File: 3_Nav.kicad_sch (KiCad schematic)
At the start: 37 parts, among them J401 Screw_Terminal_01x04, SW401 SW_Push, SW402 SW_Push, U401 LPS22HH, U402 MS5607, U403 STM32F412RGTx, U404 ICM-42688-P, U405 LSM6DSO32TR, Y401 YXC YSX321SL, Y402 Seiko SC-32S

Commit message: Add files via upload
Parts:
- U404: symbol ICM-42688-P:ICM-42688-P -> Polaris_symbols:ICM-42688-P
- U405: symbol LSM6DSO32TR:LSM6DSO32TR -> Polaris_symbols:LSM6DSO32TR
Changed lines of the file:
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@@
 	)
 	(symbol
-		(lib_id "LSM6DSO32TR:LSM6DSO32TR")
+		(lib_id "Polaris_symbols:LSM6DSO32TR")
 		(at 233.68 138.43 0)
 		(unit 1)
@@
 	)
 	(symbol
-		(lib_id "ICM-42688-P:ICM-42688-P")
+		(lib_id "Polaris_symbols:ICM-42688-P")
 		(at 226.06 81.28 0)
 		(unit 1)

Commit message: Added symbols and footprints Changed schematic to use footprints and symbols from added symbols and footprints
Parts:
- R407, R408: footprint (none) -> Resistor_SMD:R_0603_1608Metric
- SW401, SW402: footprint (none) -> Button_Switch_THT:SW_PUSH_6mm
- U401: footprint LPS22HHTR:HLGA-10L_2X2X0P73_STM -> Polaris:LPS22HH
- U404: footprint ICM42688-P:PQFN50P300X250X97-14N -> Polaris:ICM-42688-P
- U405: footprint LSM6DSO32TR:LSM6DSO32TR -> Polaris:LSM6DSO32TR

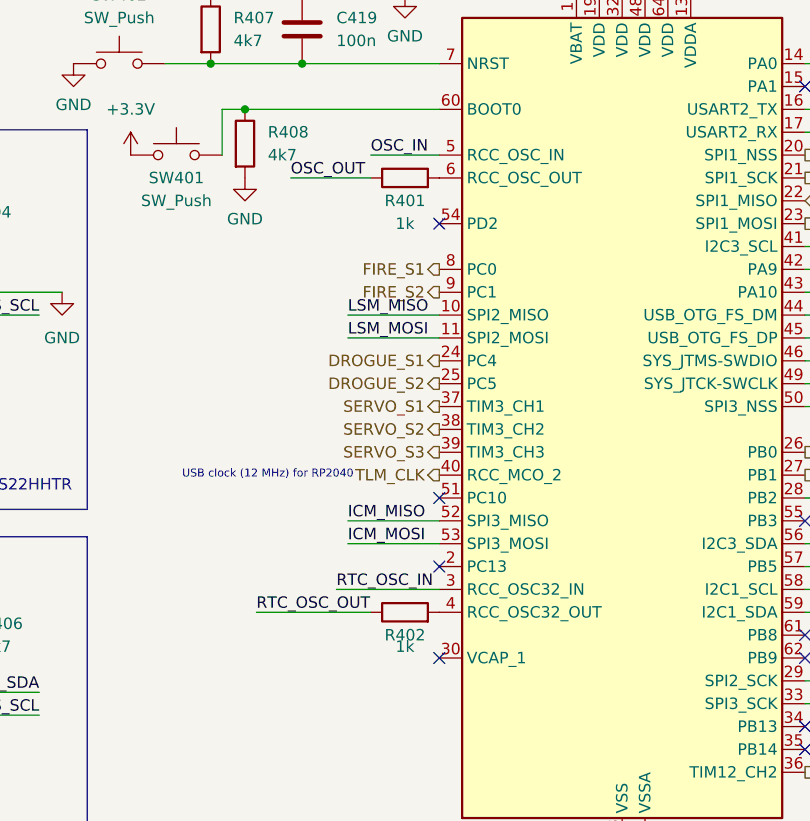
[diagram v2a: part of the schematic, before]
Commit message: Changed oscillator series resistors to DNP
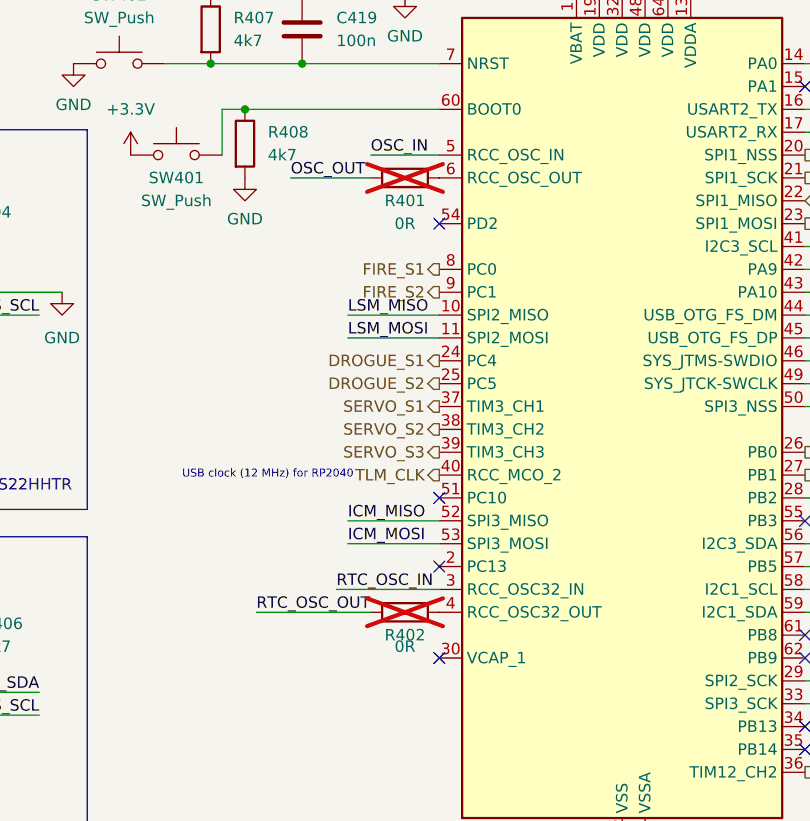
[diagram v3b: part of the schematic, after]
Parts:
- R401, R402: value 1k -> 0R; now not fitted
- Y401: footprint (none) -> Crystal:Crystal_SMD_3225-4Pin_3.2x2.5mm
- Y402: footprint (none) -> Crystal:Crystal_SMD_3215-2Pin_3.2x1.5mm
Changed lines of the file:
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@@
 			)
 		)
-		(property "Footprint" ""
+		(property "Footprint" "Crystal:Crystal_SMD_3225-4Pin_3.2x2.5mm"
 			(at 41.91 175.26 0)
 			(hide yes)
@@
 		(on_board yes)
 		(in_pos_files yes)
-		(dnp no)
+		(dnp yes)
 		(property "Reference" "R402"
 			(at 113.03 135.89 90)
@@
 			)
 		)
-		(property "Value" "1k"
+		(property "Value" "0R"
 			(at 113.03 137.16 90)
 			(show_name no)
@@
 		(on_board yes)
 		(in_pos_files yes)
-		(dnp no)
+		(dnp yes)
 		(property "Reference" "R401"
 			(at 113.03 87.63 90)
@@
 			)
 		)
-		(property "Value" "1k"
+		(property "Value" "0R"
 			(at 113.03 90.17 90)
 			(show_name no)
@@
 			)
 		)
-		(property "Footprint" ""
+		(property "Footprint" "Crystal:Crystal_SMD_3215-2Pin_3.2x1.5mm"
 			(at 90.17 175.26 0)
 			(hide yes)

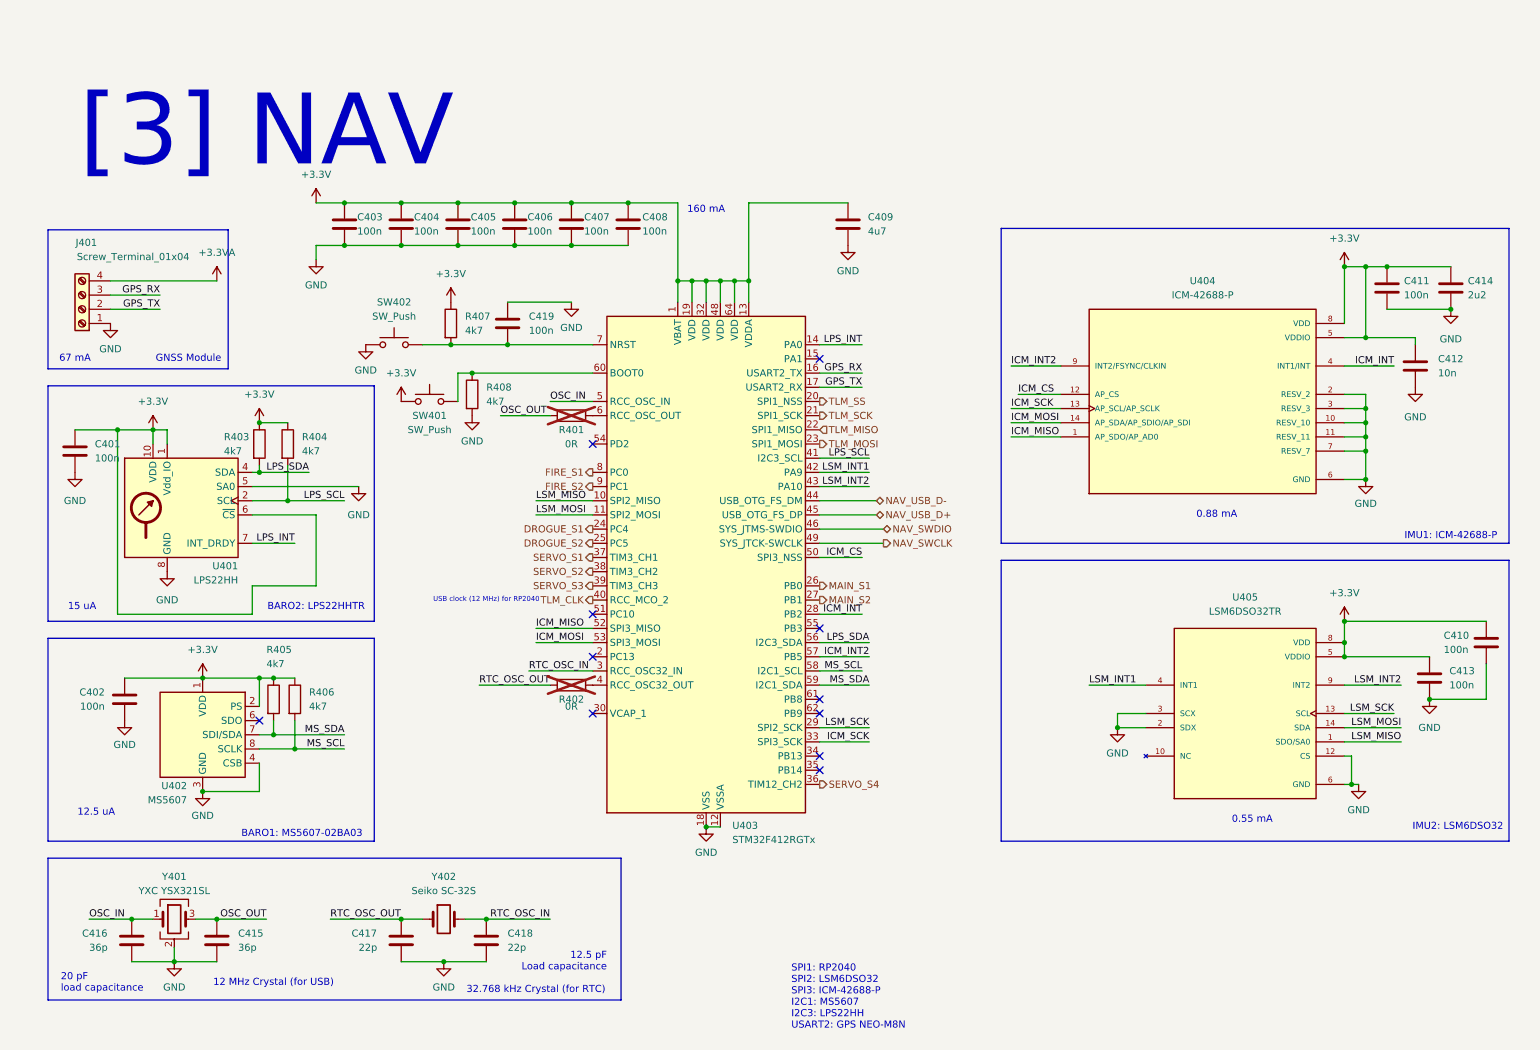
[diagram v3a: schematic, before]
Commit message: Added status LEDs and buzzer for indication
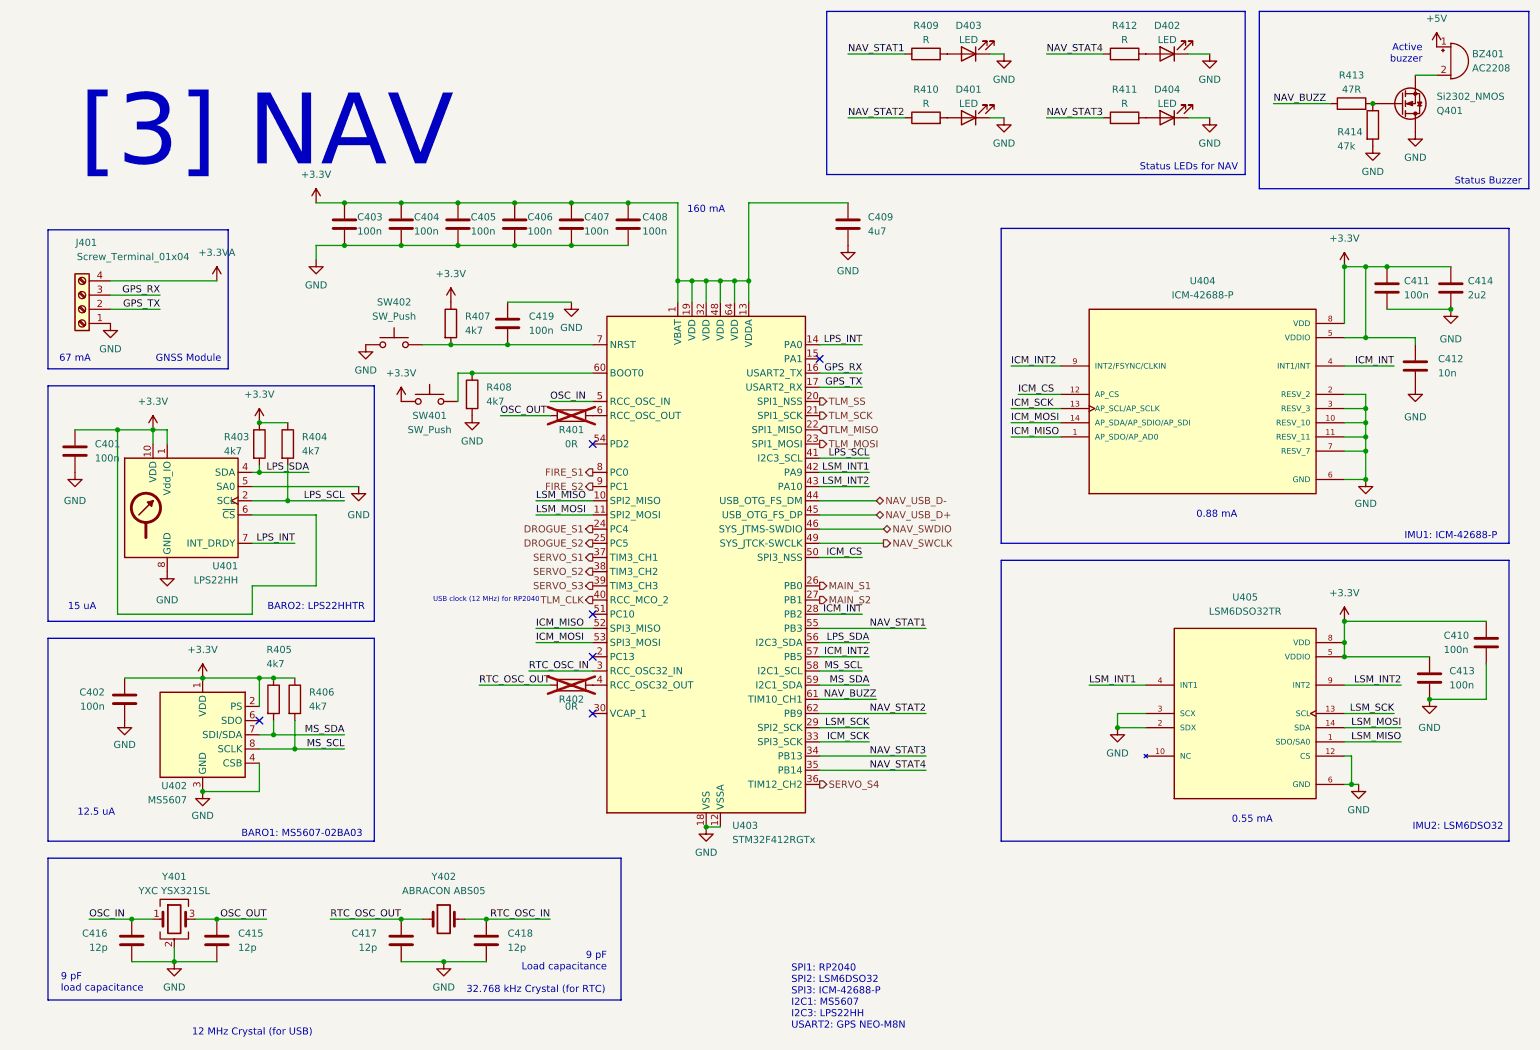
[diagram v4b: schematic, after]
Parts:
- added BZ401: AC2208, symbol Device:Buzzer
- added D401, D402, D403, D404: LED, symbol Device:LED
- added Q401: Si2302_NMOS, symbol Device:Q_NMOS
- added R409, R410, R411, R412: R, Resistor_SMD:R_0603_1608Metric, symbol Device:R
- added R413: 47R, symbol Device:R
- added R414: 47k, symbol Device:R
- C415, C416: value 36p -> 12p
- C417, C418: value 22p -> 12p
- Y402: value Seiko SC-32S -> ABRACON ABS05
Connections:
- net GND: now also D401.1 (K), D402.1 (K), D403.1 (K), D404.1 (K), Q401.D, R414.2
- net NAV_STAT3: now reaches U403.34 (PB13)
- net NAV_STAT3: now also R411.1
- net NAV_STAT4: now reaches U403.35 (PB14)
- net NAV_STAT4: now also R412.1
- net NAV_STAT1: now reaches U403.55 (PB3)
- net NAV_STAT1: now also R409.1
- net NAV_BUZZ: now reaches U403.61 (PB8)
- net NAV_BUZZ: now also R413.1
- net NAV_STAT2: now reaches U403.62 (PB9)
- net NAV_STAT2: now also R410.1
- new net: D401.2 (A), R410.2
- new net: D404.2 (A), R411.2
- new net: Q401.G, R413.2, R414.1
- new net: BZ401.2 (-), Q401.S
- new net: D402.2 (A), R412.2
- new net: D403.2 (A), R409.2
- new net +5V: BZ401.1 (+)
- no-connect marks 11 -> 6
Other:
- note added: "9 pF Load capacitance"
- note added: "9 pF load capacitance"
- note added: "Active buzzer"
- note added: "Status Buzzer"
- note added: "Status LEDs for NAV"
- note removed: "12.5 pF Load capacitance"
- note removed: "20 pF load capacitance"

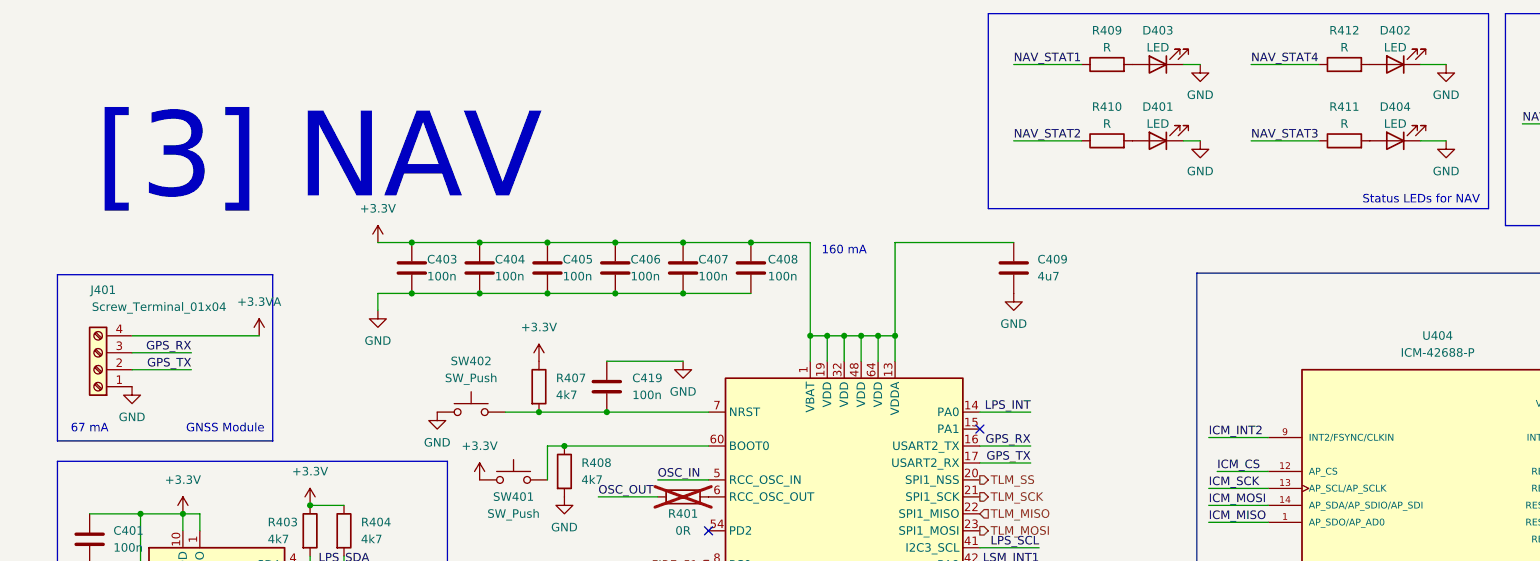
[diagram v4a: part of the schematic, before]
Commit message: Redid ESD protection because the previous chip couldn't handle 9V from USB-PD Finished status indication sections
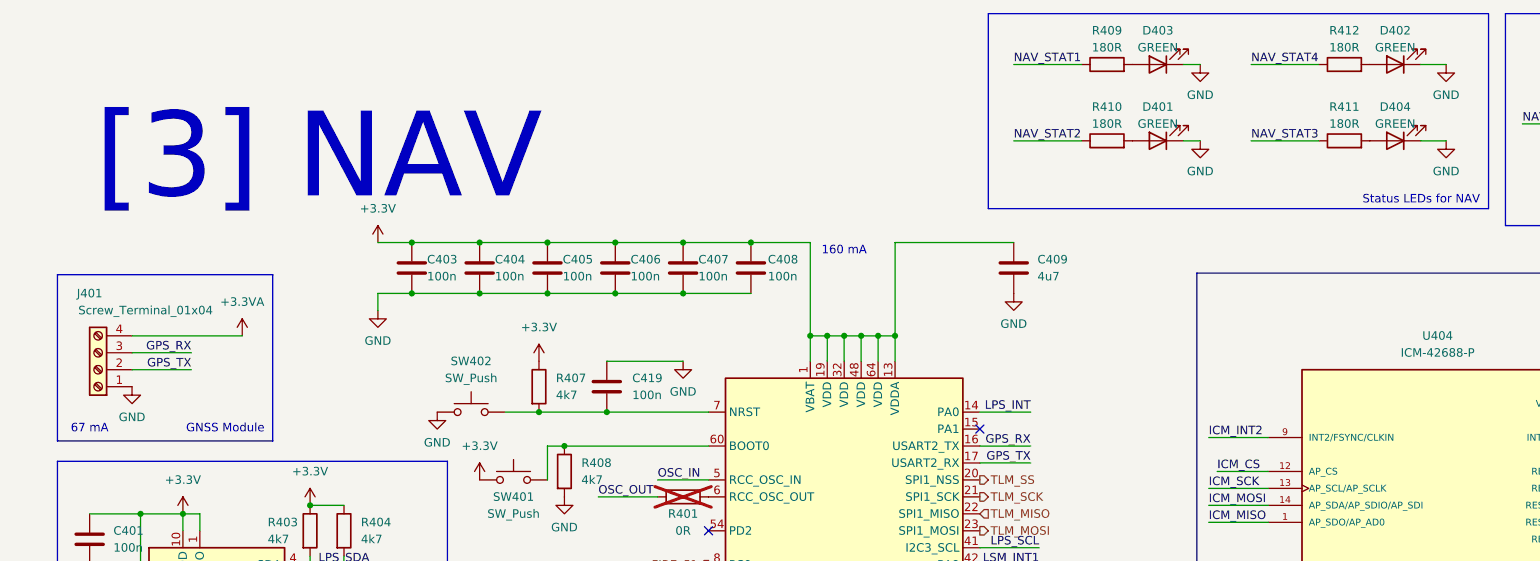
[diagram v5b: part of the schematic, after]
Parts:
- D401, D402, D403, D404: value LED -> GREEN; footprint (none) -> LED_SMD:LED_0603_1608Metric
- R409, R410, R411, R412: value R -> 180R
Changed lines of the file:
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@@
 	)
 	(rectangle
-		(start 51.562 51.816)
-		(end 19.304 76.708)
+		(start 19.304 51.816)
+		(end 51.562 76.708)
 		(stroke
 			(width 0)
@@
 	(wire
 		(pts
-			(xy 30.48 60.96) (xy 49.53 60.96)
+			(xy 30.48 60.96) (xy 46.99 60.96)
 		)
 		(stroke
@@
 			)
 		)
-		(property "Value" "R"
+		(property "Value" "180R"
 			(at 176.53 29.21 90)
 			(show_name no)
@@
 			)
 		)
-		(property "Value" "R"
+		(property "Value" "180R"
 			(at 212.09 29.21 90)
 			(show_name no)
@@
 			)
 		)
-		(property "Value" "LED"
+		(property "Value" "GREEN"
 			(at 184.15 29.21 0)
 			(show_name no)
@@
 			)
 		)
-		(property "Footprint" ""
+		(property "Footprint" "LED_SMD:LED_0603_1608Metric"
 			(at 184.15 31.75 0)
 			(hide yes)
@@
 			)
 		)
-		(property "Value" "R"
+		(property "Value" "180R"
 			(at 212.09 17.78 90)
 			(show_name no)
@@
 			)
 		)
-		(property "Value" "R"
+		(property "Value" "180R"
 			(at 176.53 17.78 90)
 			(show_name no)
@@
 		(dnp no)
 		(property "Reference" "J401"
-			(at 26.162 54.102 0)
+			(at 24.13 54.61 0)
 			(show_name no)
 			(do_not_autoplace no)
@@
 		)
 		(property "Value" "Screw_Terminal_01x04"
-			(at 34.544 56.642 0)
+			(at 32.512 57.15 0)
 			(show_name no)
 			(do_not_autoplace no)
@@
 			)
 		)
-		(property "Value" "LED"
+		(property "Value" "GREEN"
 			(at 184.15 17.78 0)
 			(show_name no)
@@
 			)
 		)
-		(property "Footprint" ""
+		(property "Footprint" "LED_SMD:LED_0603_1608Metric"
 			(at 184.15 20.32 0)
 			(hide yes)
@@
 			)
 		)
-		(property "Value" "LED"
+		(property "Value" "GREEN"
 			(at 219.71 17.78 0)
 			(show_name no)
@@
 			)
 		)
-		(property "Footprint" ""
+		(property "Footprint" "LED_SMD:LED_0603_1608Metric"
 			(at 219.71 20.32 0)
 			(hide yes)
@@
 	(symbol
 		(lib_id "power:+3.3VA")
-		(at 49.53 60.96 0)
+		(at 46.99 60.96 0)
 		(unit 1)
 		(body_style 1)
@@
 		(fields_autoplaced yes)
 		(property "Reference" "#PWR0421"
-			(at 49.53 64.77 0)
+			(at 46.99 64.77 0)
 			(hide yes)
 			(show_name no)
@@
 		)
 		(property "Value" "+3.3VA"
-			(at 49.53 55.88 0)
+			(at 46.99 55.88 0)
 			(show_name no)
 			(do_not_autoplace no)
@@
 		)
 		(property "Footprint" ""
-			(at 49.53 60.96 0)
+			(at 46.99 60.96 0)
 			(hide yes)
 			(show_name no)
@@
 		)
 		(property "Datasheet" ""
-			(at 49.53 60.96 0)
+			(at 46.99 60.96 0)
 			(hide yes)
 			(show_name no)
@@
 		)
 		(property "Description" "Power symbol creates a global label with name \"+3.3VA\""
-			(at 49.53 60.96 0)
+			(at 46.99 60.96 0)
 			(hide yes)
 			(show_name no)
@@
 			)
 		)
-		(property "Value" "LED"
+		(property "Value" "GREEN"
 			(at 219.71 29.21 0)
 			(show_name no)
@@
 			)
 		)
-		(property "Footprint" ""
+		(property "Footprint" "LED_SMD:LED_0603_1608Metric"
 			(at 219.71 31.75 0)
 			(hide yes)
